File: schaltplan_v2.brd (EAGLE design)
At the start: 100 x 80 mm, 42 parts, among them T1 2N3565, T2 2N3565, T3 2N3565, T4 2N3565, T5 2N3565, T6 2N3565, T7 2N3565, T8 2N3565

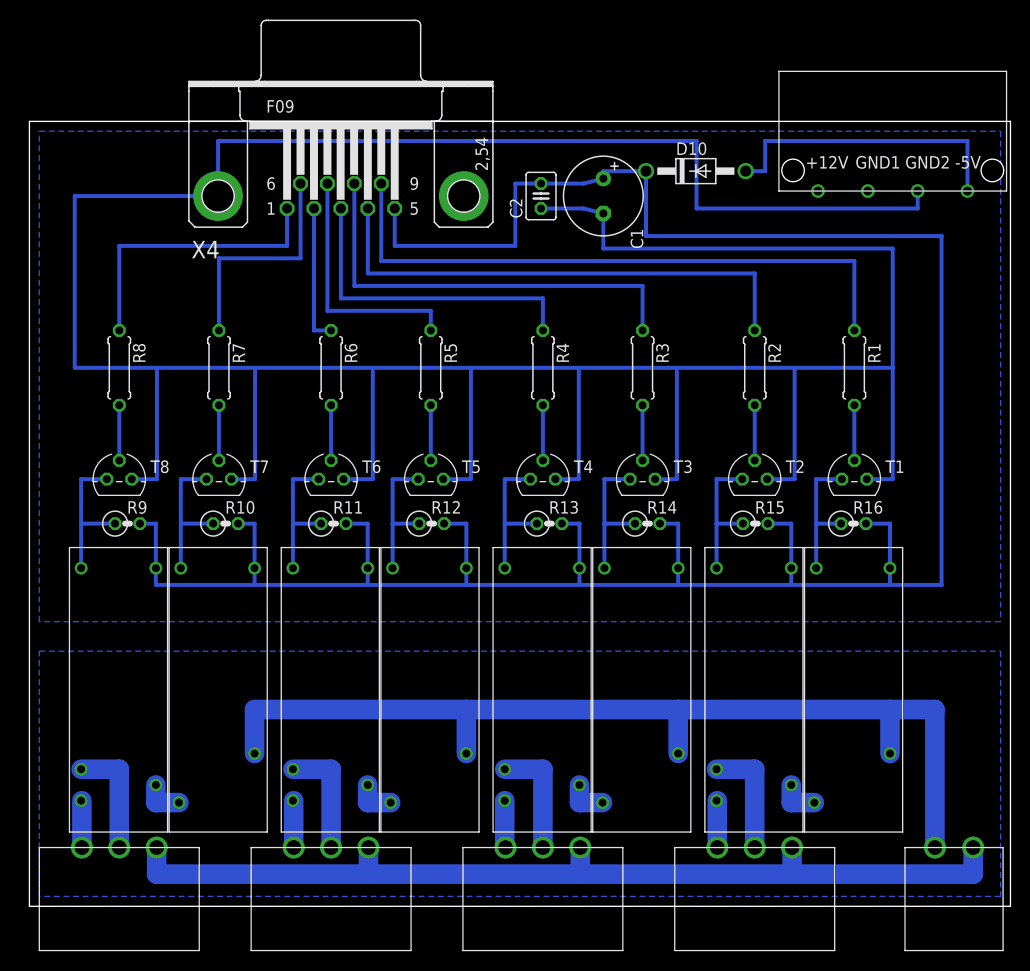
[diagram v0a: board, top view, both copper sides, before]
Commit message: 24367dfa: add drill holes and replace changed relais
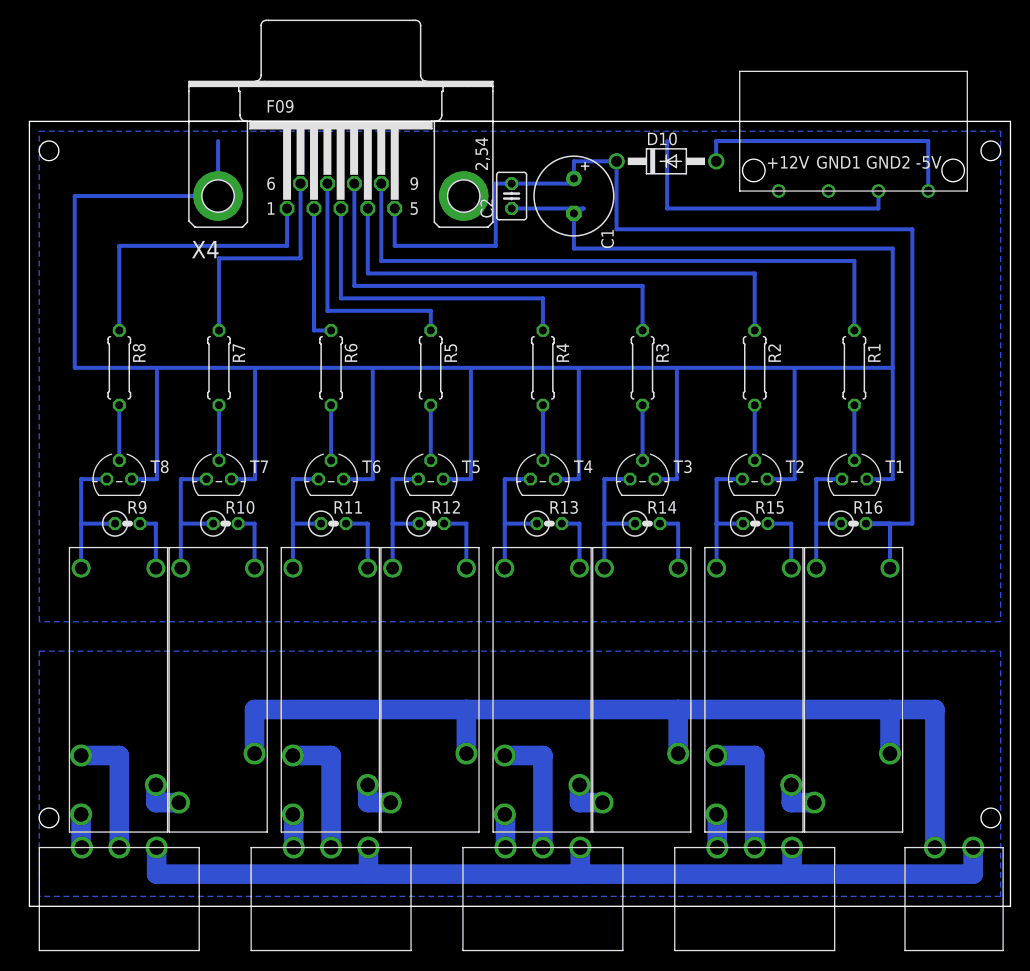
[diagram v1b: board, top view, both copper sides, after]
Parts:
- moved U$14 4.00 mm to (84.0, 79.0)
- moved D10 3.16 mm to (64.9, 75.9)
- moved C1 3.00 mm to (55.5, 72.4)
- moved C2 3.00 mm to (49.1, 72.4)
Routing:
- net N$24: track 255.4 -> 159.6 mm
- net GND: track 364.4 -> 319.7 mm
- net N$7: track 30.8 -> 28.8 mm
- net N$42: track 4.86 -> 3.46 mm
- net N$30: track 4.86 -> 3.46 mm
- net N$2: track 4.86 -> 3.46 mm
- net N$16: track 4.86 -> 3.46 mm
- net N$43: track 11.9 -> 13.3 mm
- net N$31: track 11.9 -> 13.3 mm
- net N$3: track 11.9 -> 13.3 mm
- net N$17: track 11.9 -> 13.3 mm

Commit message: 24367dfa: add label text
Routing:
- net N$38: track 63.2 -> 15.0 mm
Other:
- board size 100 x 80 mm -> 101 x 80 mm
- board text added: "n39_rollladensteuerung_v2 (c) netz39"
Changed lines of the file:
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@@
 <layers>
 <layer number="1" name="Top" color="4" fill="1" visible="no" active="yes"/>
-<layer number="16" name="Bottom" color="1" fill="1" visible="no" active="yes"/>
-<layer number="17" name="Pads" color="2" fill="1" visible="no" active="yes"/>
+<layer number="16" name="Bottom" color="1" fill="1" visible="yes" active="yes"/>
+<layer number="17" name="Pads" color="2" fill="1" visible="yes" active="yes"/>
 <layer number="18" name="Vias" color="2" fill="1" visible="no" active="yes"/>
-<layer number="19" name="Unrouted" color="6" fill="1" visible="no" active="yes"/>
+<layer number="19" name="Unrouted" color="6" fill="1" visible="yes" active="yes"/>
 <layer number="20" name="Dimension" color="15" fill="1" visible="yes" active="yes"/>
 <layer number="21" name="tPlace" color="7" fill="1" visible="yes" active="yes"/>
@@
 <wire x1="100" y1="80" x2="0" y2="80" width="0" layer="20"/>
 <wire x1="0" y1="80" x2="0" y2="0" width="0" layer="20"/>
-<wire x1="100" y1="-0.01" x2="0" y2="-0.01" width="0" layer="20"/>
+<wire x1="100" y1="-0.01" x2="-1" y2="-0.01" width="0" layer="20"/>
 <hole x="2" y="77" drill="2"/>
 <hole x="98" y="77" drill="2"/>
 <hole x="98" y="9" drill="2"/>
 <hole x="2" y="9" drill="2"/>
+<text x="97" y="31" size="1.5" layer="16" font="vector" rot="R90">n39_rollladensteuerung_v2
+(c) netz39</text>
 </plain>
 <attributes>
@@
 <contactref element="X4" pad="9"/>
 <wire x1="84.09" y1="58.69" x2="84.09" y2="65.77" width="0.4064" layer="16"/>
-<wire x1="84.09" y1="65.77" x2="35.8648" y2="65.77" width="0.4064" layer="16"/>
 <wire x1="35.8648" y1="65.77" x2="35.8648" y2="73.66" width="0.4064" layer="16"/>
+<wire x1="35.8648" y1="65.77" x2="84.09" y2="65.77" width="0" layer="19" extent="16-16"/>
 </signal>
 <signal name="GND2">
@@
 </board>
 </drawing>
+<compatibility>
+<note version="6.3" minversion="6.2.2" severity="warning">
+Since Version 6.2.2 text objects can contain more than one line,
+which will not be processed correctly with this version.
+</note>
+</compatibility>
 </eagle>

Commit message: minor fixes again
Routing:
- net N$24: track 159.6 -> 263.6 mm
- net N$38: track 15.0 -> 63.2 mm
- net GND: track 319.7 -> 361.0 mm
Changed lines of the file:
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@@
 <layers>
 <layer number="1" name="Top" color="4" fill="1" visible="no" active="yes"/>
-<layer number="16" name="Bottom" color="1" fill="1" visible="yes" active="yes"/>
+<layer number="16" name="Bottom" color="1" fill="1" visible="no" active="yes"/>
 <layer number="17" name="Pads" color="2" fill="1" visible="yes" active="yes"/>
 <layer number="18" name="Vias" color="2" fill="1" visible="no" active="yes"/>
-<layer number="19" name="Unrouted" color="6" fill="1" visible="yes" active="yes"/>
+<layer number="19" name="Unrouted" color="6" fill="1" visible="no" active="yes"/>
 <layer number="20" name="Dimension" color="15" fill="1" visible="yes" active="yes"/>
 <layer number="21" name="tPlace" color="7" fill="1" visible="yes" active="yes"/>
@@
 <hole x="98" y="9" drill="2"/>
 <hole x="2" y="9" drill="2"/>
-<text x="97" y="31" size="1.5" layer="16" font="vector" rot="R90">n39_rollladensteuerung_v2
+<text x="98" y="31" size="1.5" layer="16" font="vector" rot="R90">n39_rollladensteuerung_v2
 (c) netz39</text>
 </plain>
@@
 <contactref element="U$7" pad="P$2"/>
 <contactref element="U$8" pad="P$2"/>
-<wire x1="56.07" y1="39" x2="56.07" y2="34.46" width="0.4064" layer="16"/>
-<wire x1="66.13" y1="39" x2="66.13" y2="34.46" width="0.4064" layer="16"/>
-<wire x1="44.54" y1="39" x2="44.54" y2="34.46" width="0.4064" layer="16"/>
-<wire x1="34.48" y1="39" x2="34.48" y2="34.46" width="0.4064" layer="16"/>
 <wire x1="87.72" y1="39" x2="87.72" y2="34.46" width="0.4064" layer="16"/>
-<wire x1="22.95" y1="39" x2="22.95" y2="34.46" width="0.4064" layer="16"/>
-<wire x1="12.89" y1="34.46" x2="12.97" y2="34.46" width="0.4064" layer="16"/>
-<wire x1="77.66" y1="34.46" x2="77.74" y2="34.46" width="0.4064" layer="16"/>
-<wire x1="47.53" y1="73.66" x2="49.15" y2="73.66" width="0.4064" layer="16"/>
 <contactref element="X4" pad="5"/>
-<wire x1="47.53" y1="73.66" x2="47.53" y2="67.31" width="0.4064" layer="16"/>
-<wire x1="47.53" y1="67.31" x2="37.2364" y2="67.31" width="0.4064" layer="16"/>
-<wire x1="37.2364" y1="67.31" x2="37.2364" y2="71.12" width="0.4064" layer="16"/>
 <contactref element="R9" pad="2"/>
 <contactref element="R10" pad="2"/>
@@
 <contactref element="R16" pad="2"/>
 <wire x1="85.27" y1="39" x2="87.72" y2="39" width="0.4064" layer="16"/>
-<wire x1="75.27" y1="39" x2="77.66" y2="39" width="0.4064" layer="16"/>
-<wire x1="77.66" y1="39" x2="77.66" y2="34.46" width="0.4064" layer="16"/>
+<wire x1="85.27" y1="39" x2="92" y2="39" width="0.4064" layer="16"/>
+<wire x1="92" y1="39" x2="92" y2="32" width="0.4064" layer="16"/>
+<wire x1="92" y1="32" x2="77.66" y2="32" width="0.4064" layer="16"/>
+<wire x1="77.66" y1="32" x2="77.66" y2="34.46" width="0.4064" layer="16"/>
+<wire x1="66.13" y1="34.46" x2="66.13" y2="32" width="0.4064" layer="16"/>
+<wire x1="66.13" y1="32" x2="77.66" y2="32" width="0.4064" layer="16"/>
+<wire x1="56.07" y1="34.46" x2="56.07" y2="32" width="0.4064" layer="16"/>
+<wire x1="56.07" y1="32" x2="66.13" y2="32" width="0.4064" layer="16"/>
+<wire x1="44.54" y1="34.46" x2="44.54" y2="32" width="0.4064" layer="16"/>
+<wire x1="44.54" y1="32" x2="56.07" y2="32" width="0.4064" layer="16"/>
+<wire x1="34.48" y1="34.46" x2="34.48" y2="32" width="0.4064" layer="16"/>
+<wire x1="34.48" y1="32" x2="44.54" y2="32" width="0.4064" layer="16"/>
+<wire x1="22.95" y1="34.46" x2="22.95" y2="32" width="0.4064" layer="16"/>
+<wire x1="22.95" y1="32" x2="34.48" y2="32" width="0.4064" layer="16"/>
+<wire x1="12.89" y1="34.46" x2="12.89" y2="32" width="0.4064" layer="16"/>
+<wire x1="12.89" y1="32" x2="22.95" y2="32" width="0.4064" layer="16"/>
 <wire x1="11.27" y1="39" x2="12.89" y2="39" width="0.4064" layer="16"/>
 <wire x1="12.89" y1="39" x2="12.89" y2="34.46" width="0.4064" layer="16"/>
 <wire x1="21.27" y1="39" x2="22.95" y2="39" width="0.4064" layer="16"/>
+<wire x1="22.95" y1="39" x2="22.95" y2="34.46" width="0.4064" layer="16"/>
 <wire x1="32.27" y1="39" x2="34.48" y2="39" width="0.4064" layer="16"/>
+<wire x1="34.48" y1="39" x2="34.48" y2="34.46" width="0.4064" layer="16"/>
 <wire x1="42.27" y1="39" x2="44.54" y2="39" width="0.4064" layer="16"/>
+<wire x1="44.54" y1="39" x2="44.54" y2="34.46" width="0.4064" layer="16"/>
 <wire x1="54.27" y1="39" x2="56.07" y2="39" width="0.4064" layer="16"/>
+<wire x1="56.07" y1="39" x2="56.07" y2="34.46" width="0.4064" layer="16"/>
 <wire x1="64.27" y1="39" x2="66.13" y2="39" width="0.4064" layer="16"/>
-<wire x1="49.15" y1="73.66" x2="55.5" y2="73.66" width="0.4064" layer="16"/>
-<wire x1="55.5" y1="73.66" x2="55.5" y2="74.168" width="0.4064" layer="16"/>
-<wire x1="59.85" y1="75.93" x2="55.5" y2="75.93" width="0.4064" layer="16"/>
-<wire x1="55.5" y1="75.93" x2="55.5" y2="74.168" width="0.4064" layer="16"/>
-<wire x1="85.27" y1="39" x2="90" y2="39" width="0.4064" layer="16"/>
-<wire x1="90" y1="39" x2="90" y2="69" width="0.4064" layer="16"/>
-<wire x1="90" y1="69" x2="59.85" y2="69" width="0.4064" layer="16"/>
-<wire x1="59.85" y1="69" x2="59.85" y2="75.93" width="0.4064" layer="16"/>
-<wire x1="85.27" y1="39" x2="77.66" y2="39" width="0" layer="19" extent="16-16"/>
-<wire x1="66.13" y1="39" x2="75.27" y2="39" width="0" layer="19" extent="16-16"/>
-<wire x1="56.07" y1="39" x2="64.27" y2="39" width="0" layer="19" extent="16-16"/>
-<wire x1="44.54" y1="39" x2="54.27" y2="39" width="0" layer="19" extent="16-16"/>
-<wire x1="34.48" y1="39" x2="42.27" y2="39" width="0" layer="19" extent="16-16"/>
-<wire x1="22.95" y1="39" x2="32.27" y2="39" width="0" layer="19" extent="16-16"/>
-<wire x1="12.89" y1="39" x2="21.27" y2="39" width="0" layer="19" extent="16-16"/>
+<wire x1="66.13" y1="39" x2="66.13" y2="34.46" width="0.4064" layer="16"/>
+<wire x1="75.27" y1="39" x2="77.66" y2="39" width="0.4064" layer="16"/>
+<wire x1="77.66" y1="39" x2="77.66" y2="34.46" width="0.4064" layer="16"/>
+<wire x1="37.2364" y1="76" x2="49.15" y2="76" width="0.4064" layer="16"/>
+<wire x1="49.15" y1="76" x2="55.5" y2="76" width="0.4064" layer="16"/>
+<wire x1="55.5" y1="76" x2="60" y2="76" width="0.4064" layer="16"/>
+<wire x1="60" y1="75.93" x2="59.85" y2="75.93" width="0.4064" layer="16"/>
+<wire x1="55.5" y1="74.168" x2="55.5" y2="76" width="0.4064" layer="16"/>
+<wire x1="49.15" y1="73.66" x2="49.15" y2="76" width="0.4064" layer="16"/>
+<wire x1="37.2364" y1="71.12" x2="37.2364" y2="76" width="0.4064" layer="16"/>
+<wire x1="60" y1="76" x2="60" y2="75.93" width="0.4064" layer="16"/>
+<wire x1="60" y1="75.93" x2="60" y2="69" width="0.4064" layer="16"/>
+<wire x1="60" y1="69" x2="92" y2="69" width="0.4064" layer="16"/>
+<wire x1="92" y1="69" x2="92" y2="39" width="0.4064" layer="16"/>
 </signal>
 <signal name="GND">
@@
 <wire x1="86.54" y1="71.12" x2="65" y2="71.12" width="0.4064" layer="16"/>
 <wire x1="65" y1="71.12" x2="65" y2="78" width="0.4064" layer="16"/>
-<wire x1="19.2278" y1="78" x2="19.2278" y2="72.39" width="0.4064" layer="16"/>
-<wire x1="49.15" y1="71.12" x2="56.5" y2="71.12" width="0.4064" layer="16"/>
-<wire x1="56.5" y1="71.12" x2="55.5" y2="70.612" width="0.4064" layer="16"/>
+<wire x1="19.2278" y1="76" x2="19.2278" y2="72.39" width="0.4064" layer="16"/>
+<wire x1="49.15" y1="71.12" x2="55.5" y2="71.12" width="0.4064" layer="16"/>
+<wire x1="55.5" y1="71.12" x2="55.5" y2="70.612" width="0.4064" layer="16"/>
 <polygon width="0.4064" layer="16">
 <vertex x="1" y="79"/>
@@
 <wire x1="88" y1="67.04" x2="55.5" y2="67.04" width="0.4064" layer="16"/>
 <wire x1="55.5" y1="67.04" x2="55.5" y2="70.612" width="0.4064" layer="16"/>
+<wire x1="20" y1="78" x2="65" y2="78" width="0.4064" layer="16"/>
 </signal>
 <signal name="N$11">
@@
 <contactref element="X4" pad="9"/>
 <wire x1="84.09" y1="58.69" x2="84.09" y2="65.77" width="0.4064" layer="16"/>
-<wire x1="35.8648" y1="65.77" x2="35.8648" y2="73.66" width="0.4064" layer="16"/>
-<wire x1="35.8648" y1="65.77" x2="84.09" y2="65.77" width="0" layer="19" extent="16-16"/>
+<wire x1="84.09" y1="65.77" x2="35.8648" y2="65.77" width="0.4064" layer="16"/>
+<wire x1="35.8648" y1="73.66" x2="35.8648" y2="65.77" width="0.4064" layer="16"/>
 </signal>
 <signal name="GND2">
@@
 </signal>
 </signals>
+<errors>
+</errors>
 </board>
 </drawing>

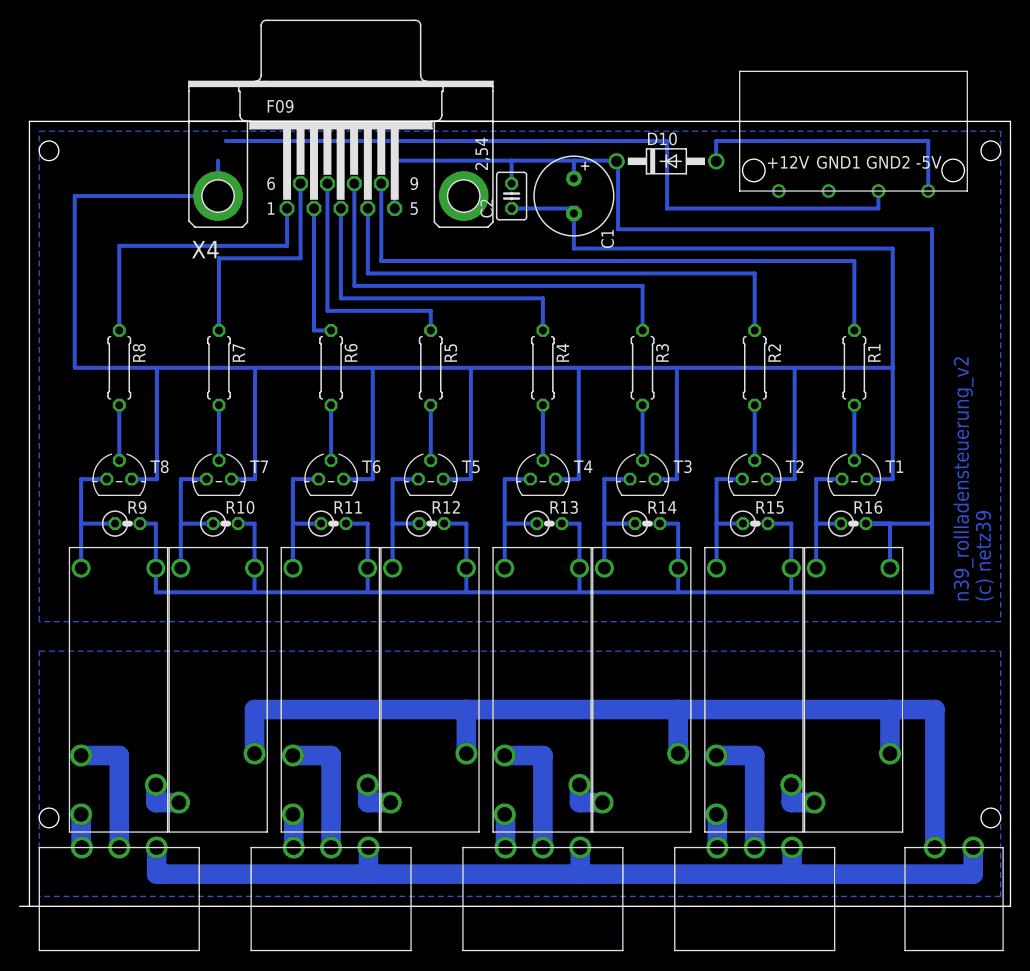
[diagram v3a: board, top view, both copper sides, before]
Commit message: rerouting and fixed drill hole distances
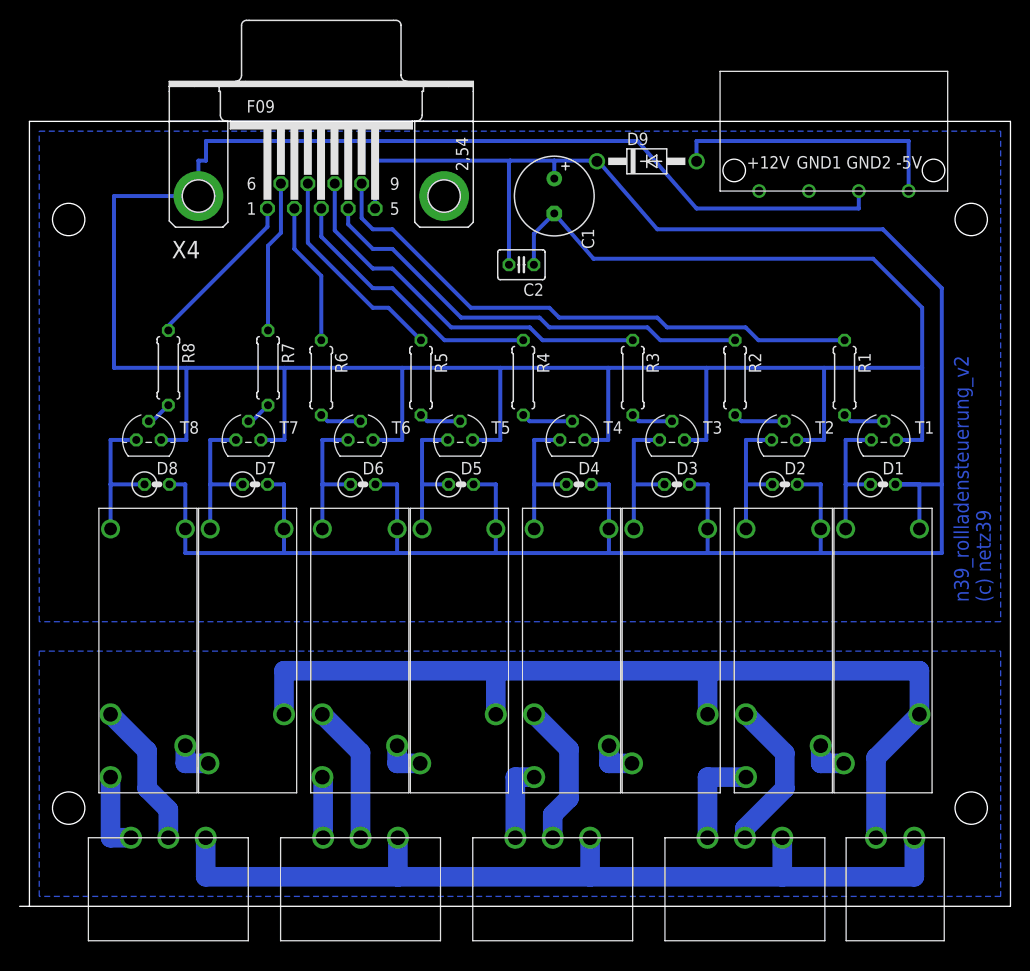
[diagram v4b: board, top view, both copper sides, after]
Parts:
- removed D10: 1N4004, diode:DO41-10
- removed R10, R11, R12, R13, R14, R15, R16, R9: (no value), rcl:0207/2V
- added D1, D2, D3, D4, D5, D6, D7, D8: (no value), rcl:0207/2V
- added D9: 1N4004, diode:DO41-10
- moved C2 7.07 mm to (50.1, 65.4), turned to 180 degrees
- moved U$9 6.08 mm to (88.2, 1.73)
- moved U$13 5.10 mm to (14.2, 1.73)
- moved R7 5.00 mm to (24.3, 54.9)
- moved R8 5.00 mm to (14.2, 54.9)
- moved T1 5.00 mm to (87.1, 47.5)
- moved T2 5.00 mm to (76.9, 47.5)
- moved T3 5.00 mm to (65.5, 47.5)
- moved T4 5.00 mm to (55.3, 47.5)
- moved T5 5.00 mm to (43.9, 47.5)
- moved T6 5.00 mm to (33.8, 47.5)
- moved T7 5.00 mm to (22.3, 47.5)
- moved T8 5.00 mm to (12.2, 47.5)
- moved U$1 5.00 mm to (82.0, 40.6)
- moved U$2 5.00 mm to (71.8, 40.6)
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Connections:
- net N$12: now also D2.1; no longer R15.1
- net N$20: now also D3.1; no longer R14.1
- net N$24: now also D1.2, D2.2, D3.2, D4.2, D5.2, D6.2, D7.2, D8.2, D9.C; no longer D10.C, R10.2, R11.2, R12.2, R13.2, R14.2, R15.2, R16.2, R9.2
- net N$25: now also D4.1; no longer R13.1
- net N$34: now also D5.1; no longer R12.1
- net N$39: now also D6.1; no longer R11.1
- net N$46: now also D7.1; no longer R10.1
- net N$51: now also D8.1; no longer R9.1
- net N$6: now also D1.1; no longer R16.1
- net N$7: now also D9.A; no longer D10.A
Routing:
- net GND: track 361.0 -> 319.8 mm
- net N$15: track 29.5 -> 16.6 mm
- net N$21: track 23.3 -> 15.5 mm
- net N$2: track 3.46 -> 10.1 mm
- net N$26: track 51.9 -> 45.9 mm
- net N$38: track 63.2 -> 57.9 mm
- net N$23: track 33.0 -> 27.8 mm
- net N$42: track 3.46 -> 8.26 mm
- net GND2: track 96.8 -> 92.1 mm
- net N$16: track 3.46 -> 8.10 mm
- net N$37: track 44.3 -> 39.8 mm
- net N$5: track 101.4 -> 96.9 mm
- net N$24: track 263.6 -> 259.7 mm
- net N$11: track 25.5 -> 21.7 mm
- net N$48: track 5.63 -> 2.68 mm
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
